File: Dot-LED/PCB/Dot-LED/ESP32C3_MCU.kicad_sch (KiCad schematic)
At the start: 1 part, among them U1 ESP32-C3

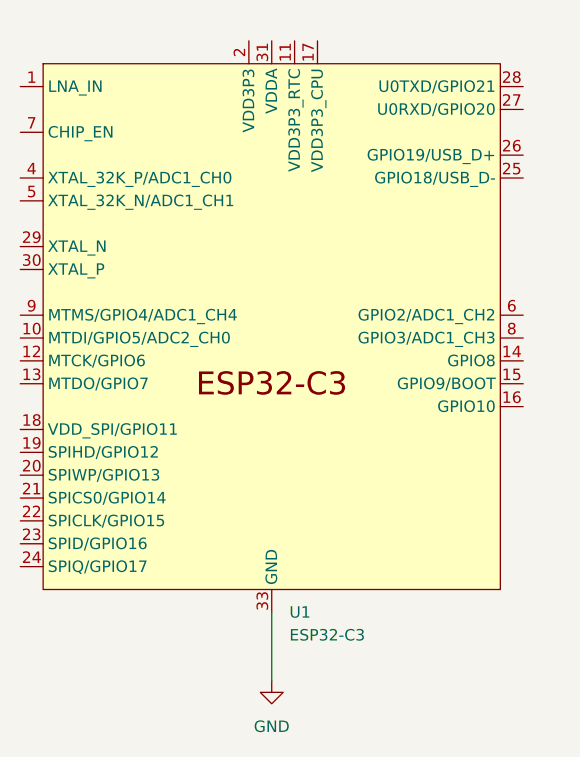
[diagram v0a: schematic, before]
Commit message: add common KiCad library using plugin
https://componentsearchengine.com/ga/downloads.php
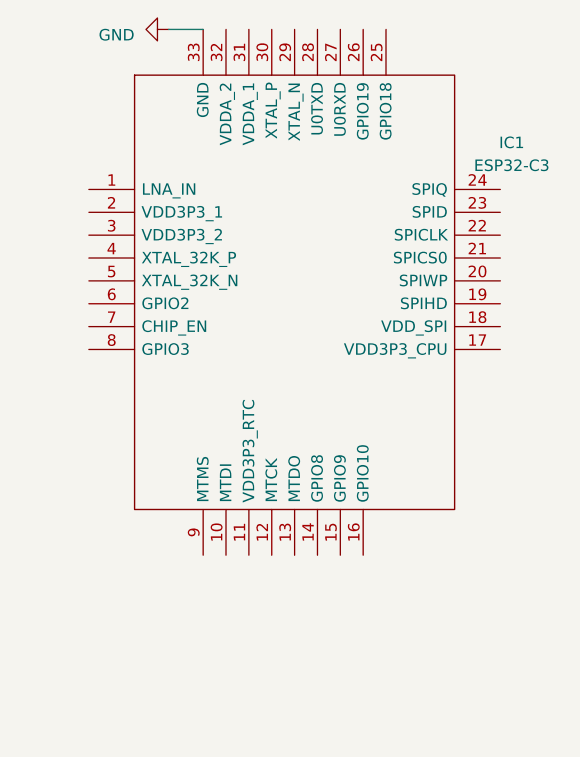
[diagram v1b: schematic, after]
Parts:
- removed U1: ESP32-C3, Package_DFN_QFN:QFN-32-1EP_5x5mm_P0.5mm_EP3.45x3.45mm, symbol Espressif:ESP32-C3
- added IC1: ESP32-C3, QFN50P500X500X90-33N-D, symbol SamacSys_Parts:ESP32-C3
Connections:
- net GND: now also IC1.33 (GND)
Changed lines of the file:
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@@
 (kicad_sch (version 20230121) (generator eeschema)
   (paper "A4")
-  (wire (pts (xy 142.24 115.57) (xy 142.24 123.19))
+  (wire (pts (xy 130.81 50.8) (xy 134.62 50.8))
     (stroke (width 0) (type default))
   )
-  (symbol (lib_id "Espressif:ESP32-C3") (at 142.24 85.09 0) (unit 1)
+  (symbol (lib_id "SamacSys_Parts:ESP32-C3") (at 121.92 68.58 0) (unit 1)
     (in_bom yes) (on_board yes) (dnp no) (fields_autoplaced)
-    (property "Reference" "U1" (at 144.1959 115.57 0)
-      (effects (font (size 1.27 1.27)) (justify left))
+    (property "Reference" "IC1" (at 168.91 63.3983 0)
+      (effects (font (size 1.27 1.27)))
     )
-    (property "Value" "ESP32-C3" (at 144.1959 118.11 0)
-      (effects (font (size 1.27 1.27)) (justify left))
+    (property "Value" "ESP32-C3" (at 168.91 65.9383 0)
+      (effects (font (size 1.27 1.27)))
     )
-    (property "Footprint" "Package_DFN_QFN:QFN-32-1EP_5x5mm_P0.5mm_EP3.45x3.45mm" (at 142.24 123.19 0)
-      (effects (font (size 1.27 1.27)) hide)
+    (property "Footprint" "QFN50P500X500X90-33N-D" (at 163.83 55.88 0)
+      (effects (font (size 1.27 1.27)) (justify left) hide)
     )
-    (property "Datasheet" "https://www.espressif.com/sites/default/files/documentation/esp32-c3_datasheet_en.pdf" (at 142.24 125.73 0)
-      (effects (font (size 1.27 1.27)) hide)
+    (property "Datasheet" "https://www.espressif.com/sites/default/files/documentation/esp32-c3_datasheet_en.pdf" (at 163.83 58.42 0)
+      (effects (font (size 1.27 1.27)) (justify left) hide)
+    )
+    (property "Description" "Ultra-Low-Power SoC with RISC-V Single-Core CPU" (at 163.83 60.96 0)
+      (effects (font (size 1.27 1.27)) (justify left) hide)
+    )
+    (property "Height" "0.9" (at 163.83 63.5 0)
+      (effects (font (size 1.27 1.27)) (justify left) hide)
+    )
+    (property "Manufacturer_Name" "Espressif Systems" (at 163.83 66.04 0)
+      (effects (font (size 1.27 1.27)) (justify left) hide)
+    )
+    (property "Manufacturer_Part_Number" "ESP32-C3" (at 163.83 68.58 0)
+      (effects (font (size 1.27 1.27)) (justify left) hide)
+    )
+    (property "Mouser Part Number" "356-ESP32-C3" (at 163.83 71.12 0)
+      (effects (font (size 1.27 1.27)) (justify left) hide)
+    )
+    (property "Mouser Price/Stock" "https://www.mouser.co.uk/ProductDetail/Espressif-Systems/ESP32-C3?qs=iLbezkQI%252BsiMXe7tMG%252Bo%2FA%3D%3D" (at 163.83 73.66 0)
+      (effects (font (size 1.27 1.27)) (justify left) hide)
+    )
+    (property "Arrow Part Number" "" (at 163.83 76.2 0)
+      (effects (font (size 1.27 1.27)) (justify left) hide)
+    )
+    (property "Arrow Price/Stock" "" (at 163.83 78.74 0)
+      (effects (font (size 1.27 1.27)) (justify left) hide)
     )
     (pin "1")
@@
     (pin "28")
     (pin "29")
+    (pin "3")
     (pin "30")
     (pin "31")
+    (pin "32")
     (pin "33")
     (pin "4")
@@
     (pin "8")
     (pin "9")
-    (pin "3")
-    (pin "32")
     (instances
       (project "Dot-LED"
         (path "/e63e39d7-6ac0-4ffd-8aa3-1841a4541b55/a9d22b06-9d00-4739-b036-54f1b218cb56"
-          (reference "U1") (unit 1)
+          (reference "IC1") (unit 1)
         )
       )
     )
   )
-  (symbol (lib_id "power:GND") (at 142.24 123.19 0) (unit 1)
+  (symbol (lib_id "power:GND") (at 130.81 50.8 270) (unit 1)
     (in_bom yes) (on_board yes) (dnp no) (fields_autoplaced)
-    (property "Reference" "#PWR01" (at 142.24 129.54 0)
+    (property "Reference" "#PWR01" (at 124.46 50.8 0)
       (effects (font (size 1.27 1.27)) hide)
     )
-    (property "Value" "GND" (at 142.24 128.27 0)
-      (effects (font (size 1.27 1.27)))
+    (property "Value" "GND" (at 127 51.435 90)
+      (effects (font (size 1.27 1.27)) (justify right))
     )
-    (property "Footprint" "" (at 142.24 123.19 0)
+    (property "Footprint" "" (at 130.81 50.8 0)
       (effects (font (size 1.27 1.27)) hide)
     )
-    (property "Datasheet" "" (at 142.24 123.19 0)
+    (property "Datasheet" "" (at 130.81 50.8 0)
       (effects (font (size 1.27 1.27)) hide)
     )

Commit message: update DotLED Sch
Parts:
- added C1, C10, C11, C2: 24nF, SamacSys_Parts:CAPC1005X55N, symbol SamacSys_Parts:0402B102K500NT
- added C3, C6: 1uF, Capacitor_SMD:C_0603_1608Metric_Pad1.08x0.95mm_HandSolder, symbol SamacSys_Parts:0402B102K500NT
- added C4, C5, C7, C8, C9: 100nf, Capacitor_SMD:C_0603_1608Metric_Pad1.08x0.95mm_HandSolder, symbol SamacSys_Parts:0402B102K500NT
- added L1: 2nH, LQG15WH0N7B02D, symbol SamacSys_Parts:LQG15HN2N0S02D
- added R1, R4: 0, RESC1608X55N, symbol SamacSys_Parts:RMCF0603ZT0R00
- added R2, R3: 15k, RESC1608X55N, symbol SamacSys_Parts:RMCF0603ZT0R00
- added S1, S2: PTS815_SJM_250_SMTR_LFS, PTS815SJM250SMTRLFS, symbol SamacSys_Parts:PTS815_SJM_250_SMTR_LFS
- added Y1: 32.768Khz, SamacSys_Parts:RH1002500012F1010TR, symbol SamacSys_Parts:RH100-25.000-12-F-1010-TR
- added Y2: RH100-40.000-12-F-1010-TR, SamacSys_Parts:RH1002500012F1010TR, symbol SamacSys_Parts:RH100-25.000-12-F-1010-TR
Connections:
- net GND: now also C1.1, C10.2, C11.1, C2.2, C3.1, C4.1, C5.1, C6.1, C7.1, C8.1, C9.1, S1.3 (NO_1), S2.3 (NO_1), Y1.2 (GND_1), Y1.4 (GND_2), Y2.2 (GND_1), Y2.4 (GND_2)
- net 3V3_VCC: now reaches IC1.11 (VDD3P3_RTC)
- net 3V3_VCC: now also IC1.17 (VDD3P3_CPU), C3.2, C4.2, C6.2, C7.2, L1.1, R2.2, R3.2
- net at IC1.2 (VDD3P3_1): now also IC1.3 (VDD3P3_2), C5.2, L1.2
- net ESP_DN: now reaches IC1.25 (GPIO18)
- net ESP_DP: now reaches IC1.26 (GPIO19)
- net at IC1.29 (XTAL_N): now also R1.1
- net at IC1.30 (XTAL_P): now also C2.1, Y2.3 (CRYSTAL_2)
- new net: C11.2, R4.2, Y1.1 (CRYSTAL_1)
- new net: C9.2, R2.1, S2.4 (NO_2)
- new net: C8.2, R3.1, S1.4 (NO_2)
- new net: C1.2, R1.2, Y2.1 (CRYSTAL_1)
- new net 32k_1: R4.1
- new net 32k_2: C10.1, Y1.3 (CRYSTAL_2)

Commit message: Update DotLED Schem
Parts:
- added R5: 1, RESC1608X55N, symbol SamacSys_Parts:RMCF0603ZT0R00
- C1, C10, C11, C2: Digi-Key_PN (none) -> CC0402JRNPO9BN240
- C3, C6: Digi-Key_PN (none) -> 1276-1102-1-ND
- IC1: Digi-Key_PN (none) -> 356-ESP32-C3
- L1: Digi-Key_PN (none) -> 81-LQG15HN2N0S02D
- R1, R4: Digi-Key_PN (none) -> 708-RMCF0603ZT0R00
- S1, S2: Digi-Key_PN (none) -> 611-PTS815SJM250SMTR
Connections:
- net 32k_1: now also IC1.4 (XTAL_32K_P)
- net 32k_2: now also IC1.5 (XTAL_32K_N)
- net D9: now reaches C9.2, R2.1, S2.4 (NO_2)
- net D9: now also IC1.15 (GPIO9)
- net EN: now reaches C8.2, R3.1, S1.4 (NO_2)
- net EN: now also IC1.7 (CHIP_EN)
- net D3: now reaches IC1.10 (MTDI)
- net D4: now reaches IC1.12 (MTCK)
- net D5: now reaches IC1.13 (MTDO)
- net D8: now reaches IC1.14 (GPIO8)
- net at IC1.27 (U0RXD): now also R5.2
- net TX_D6: now reaches IC1.28 (U0TXD)
- net D1: now reaches IC1.8 (GPIO3)
- net D2: now reaches IC1.9 (MTMS)
- new net RX_D7: R5.1
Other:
- moved on the sheet: C1, C2, R1, Y2

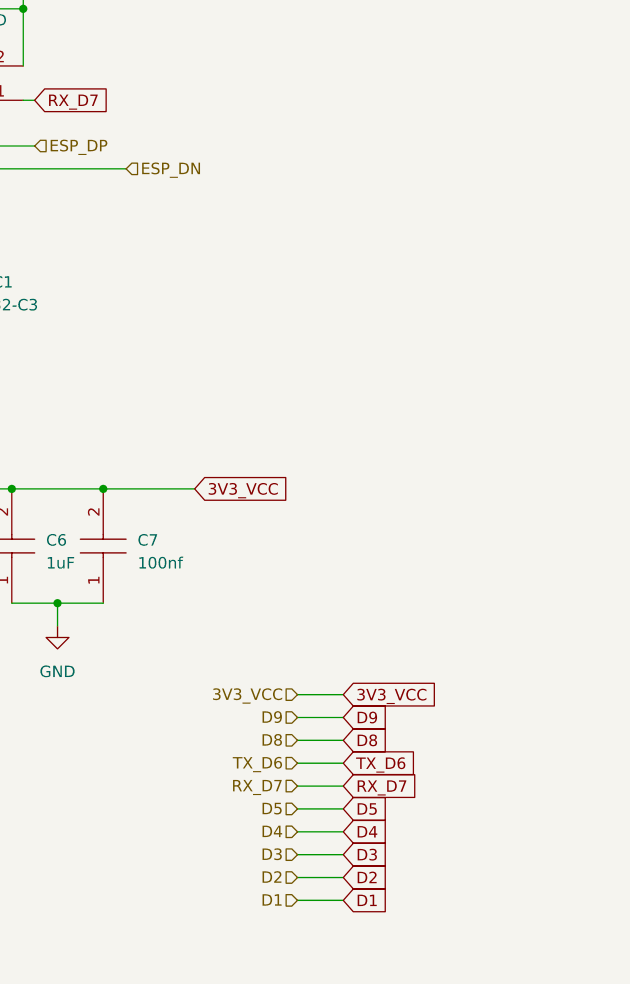
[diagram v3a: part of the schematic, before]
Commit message: update DotLED
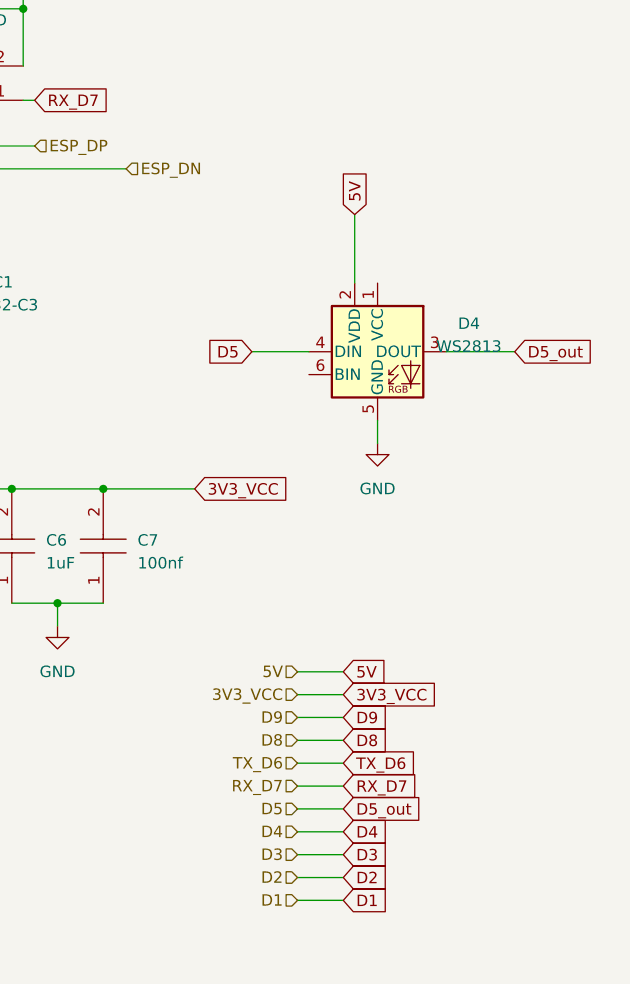
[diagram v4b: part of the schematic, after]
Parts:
- added D4: WS2813, LED_SMD:LED_WS2812_PLCC6_5.0x5.0mm_P1.6mm, symbol LED:WS2813
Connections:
- net D5: now also D4.3 (DOUT), D4.4 (DIN)
- net GND: now also D4.5 (GND)
- new net 5V: D4.2 (VDD)
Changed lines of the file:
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@@
+    (stroke (width 0) (type default))
+  )
+  (wire (pts (xy 218.44 71.12) (xy 226.06 71.12))
     (stroke (width 0) (type default))
   )
@@
     (stroke (width 0) (type default))
   )
+  (wire (pts (xy 210.82 78.74) (xy 210.82 81.28))
+    (stroke (width 0) (type default))
+  )
   (wire (pts (xy 96.52 176.53) (xy 106.68 176.53))
     (stroke (width 0) (type default))
@@
     (stroke (width 0) (type default))
   )
+  (wire (pts (xy 196.85 71.12) (xy 203.2 71.12))
+    (stroke (width 0) (type default))
+  )
   (wire (pts (xy 96.52 176.53) (xy 96.52 177.8))
     (stroke (width 0) (type default))
@@
     (stroke (width 0) (type default))
   )
+  (wire (pts (xy 201.93 121.92) (xy 207.01 121.92))
+    (stroke (width 0) (type default))
+  )
   (wire (pts (xy 110.49 133.35) (xy 110.49 124.46))
     (stroke (width 0) (type default))
@@
     (stroke (width 0) (type default))
   )
+  (wire (pts (xy 201.93 106.68) (xy 207.01 106.68))
+    (stroke (width 0) (type default))
+  )
   (wire (pts (xy 175.26 99.06) (xy 175.26 101.6))
     (stroke (width 0) (type default))
@@
     (stroke (width 0) (type default))
   )
+  (wire (pts (xy 208.28 55.88) (xy 208.28 63.5))
+    (stroke (width 0) (type default))
+  )
   (wire (pts (xy 147.32 109.22) (xy 147.32 111.76))
     (stroke (width 0) (type default))
@@
     (stroke (width 0) (type default))
   )
-  (wire (pts (xy 201.93 121.92) (xy 207.01 121.92))
-    (stroke (width 0) (type default))
-  )
   (global_label "TX_D6" (shape input) (at 207.01 116.84 0) (fields_autoplaced)
     (effects (font (size 1.27 1.27)) (justify left))
@@
     )
   )
+  (global_label "5V" (shape input) (at 208.28 55.88 90) (fields_autoplaced)
+    (effects (font (size 1.27 1.27)) (justify left))
+    (property "Intersheetrefs" "${INTERSHEET_REFS}" (at 208.28 50.6761 90)
+      (effects (font (size 1.27 1.27)) (justify left) hide)
+    )
+  )
   (global_label "32k_1" (shape input) (at 118.11 76.2 180) (fields_autoplaced)
     (effects (font (size 1.27 1.27)) (justify right))
@@
     )
   )
+  (global_label "D5" (shape input) (at 196.85 71.12 180) (fields_autoplaced)
+    (effects (font (size 1.27 1.27)) (justify right))
+    (property "Intersheetrefs" "${INTERSHEET_REFS}" (at 191.4647 71.12 0)
+      (effects (font (size 1.27 1.27)) (justify right) hide)
+    )
+  )
+  (global_label "5V" (shape input) (at 207.01 106.68 0) (fields_autoplaced)
+    (effects (font (size 1.27 1.27)) (justify left))
+    (property "Intersheetrefs" "${INTERSHEET_REFS}" (at 212.2139 106.68 0)
+      (effects (font (size 1.27 1.27)) (justify left) hide)
+    )
+  )
   (global_label "3V3_VCC" (shape input) (at 62.23 82.55 180) (fields_autoplaced)
     (effects (font (size 1.27 1.27)) (justify right))
@@
     )
   )
-  (global_label "D5" (shape input) (at 207.01 121.92 0) (fields_autoplaced)
-    (effects (font (size 1.27 1.27)) (justify left))
-    (property "Intersheetrefs" "${INTERSHEET_REFS}" (at 212.3953 121.92 0)
+  (global_label "D5_out" (shape input) (at 226.06 71.12 0) (fields_autoplaced)
+    (effects (font (size 1.27 1.27)) (justify left))
+    (property "Intersheetrefs" "${INTERSHEET_REFS}" (at 235.4366 71.12 0)
       (effects (font (size 1.27 1.27)) (justify left) hide)
     )
@@
       (effects (font (size 1.27 1.27)) (justify right) hide)
     )
+  )
+  (global_label "D5_out" (shape input) (at 207.01 121.92 0) (fields_autoplaced)
+    (effects (font (size 1.27 1.27)) (justify left))
+    (property "Intersheetrefs" "${INTERSHEET_REFS}" (at 216.3866 121.92 0)
+      (effects (font (size 1.27 1.27)) (justify left) hide)
+    )
+  )
+  (hierarchical_label "5V" (shape input) (at 201.93 106.68 180) (fields_autoplaced)
+    (effects (font (size 1.27 1.27)) (justify right))
   )
   (hierarchical_label "ESP_DP" (shape input) (at 172.72 48.26 0) (fields_autoplaced)
@@
         (path "/e63e39d7-6ac0-4ffd-8aa3-1841a4541b55/a9d22b06-9d00-4739-b036-54f1b218cb56"
           (reference "#PWR010") (unit 1)
+        )
+      )
+    )
+  )
+  (symbol (lib_id "LED:WS2813") (at 210.82 71.12 0) (unit 1)
+    (in_bom yes) (on_board yes) (dnp no) (fields_autoplaced)
+    (property "Reference" "D4" (at 220.98 67.9959 0)
+      (effects (font (size 1.27 1.27)))
+    )
+    (property "Value" "WS2813" (at 220.98 70.5359 0)
+      (effects (font (size 1.27 1.27)))
+    )
+    (property "Footprint" "LED_SMD:LED_WS2812_PLCC6_5.0x5.0mm_P1.6mm" (at 212.09 78.74 0)
+      (effects (font (size 1.27 1.27)) (justify left top) hide)
+    )
+    (property "Datasheet" "http://www.normandled.com/upload/201605/WS2813%20LED%20Datasheet.pdf" (at 213.36 80.645 0)
+      (effects (font (size 1.27 1.27)) (justify left top) hide)
+    )
+    (pin "1")
+    (pin "2")
+    (pin "3")
+    (pin "4")
+    (pin "5")
+    (pin "6")
+    (instances
+      (project "Dot-LED"
+        (path "/e63e39d7-6ac0-4ffd-8aa3-1841a4541b55/a9d22b06-9d00-4739-b036-54f1b218cb56"
+          (reference "D4") (unit 1)
         )
       )
@@
         )
       )
+    )
+  )
+  (symbol (lib_id "power:GND") (at 210.82 81.28 0) (unit 1)
+    (in_bom yes) (on_board yes) (dnp no) (fields_autoplaced)
+    (property "Reference" "#PWR04" (at 210.82 87.63 0)
+      (effects (font (size 1.27 1.27)) hide)
+    )
+    (property "Value" "GND" (at 210.82 86.36 0)
+      (effects (font (size 1.27 1.27)))
+    )
+    (property "Footprint" "" (at 210.82 81.28 0)
+      (effects (font (size 1.27 1.27)) hide)
+    )
+    (property "Datasheet" "" (at 210.82 81.28 0)
+      (effects (font (size 1.27 1.27)) hide)
+    )
+    (pin "1")
+    (instances
+      (project "Dot-LED"
+        (path "/e63e39d7-6ac0-4ffd-8aa3-1841a4541b55/a9d22b06-9d00-4739-b036-54f1b218cb56"
+          (reference "#PWR04") (unit 1)
+        )
+      )
